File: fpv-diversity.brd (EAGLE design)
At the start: 56 x 93 mm, 63 parts, among them U1 LM1881M/NOPB, U2 LM1881M/NOPB, U3 LM1881M/NOPB, U4 MAX4545CAP+, U5 LT6206CMS8PBF, U6 LM1117IMP-5.0-NOPB

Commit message: more updates
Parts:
- R13, R2, R9: device rcl:R1206 -> rcl:R0805

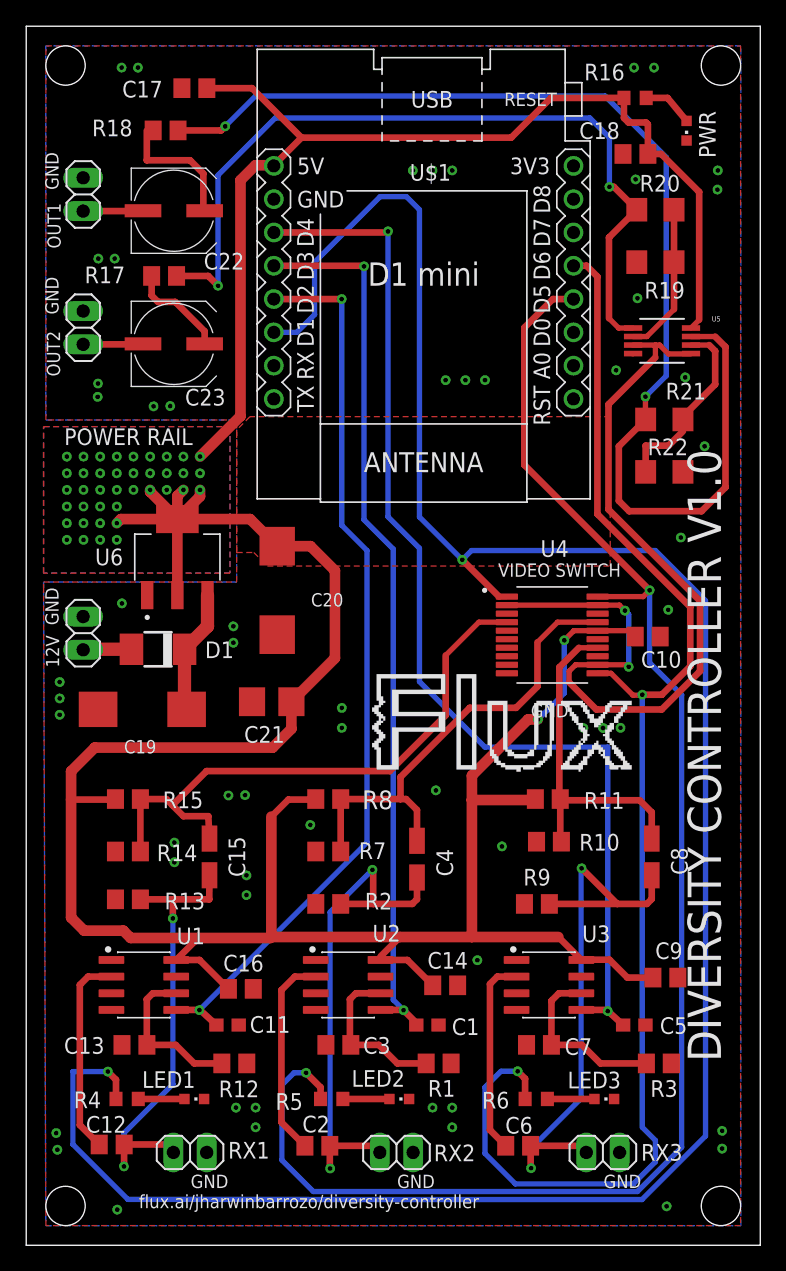
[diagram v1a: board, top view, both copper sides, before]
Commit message: board gerber updates
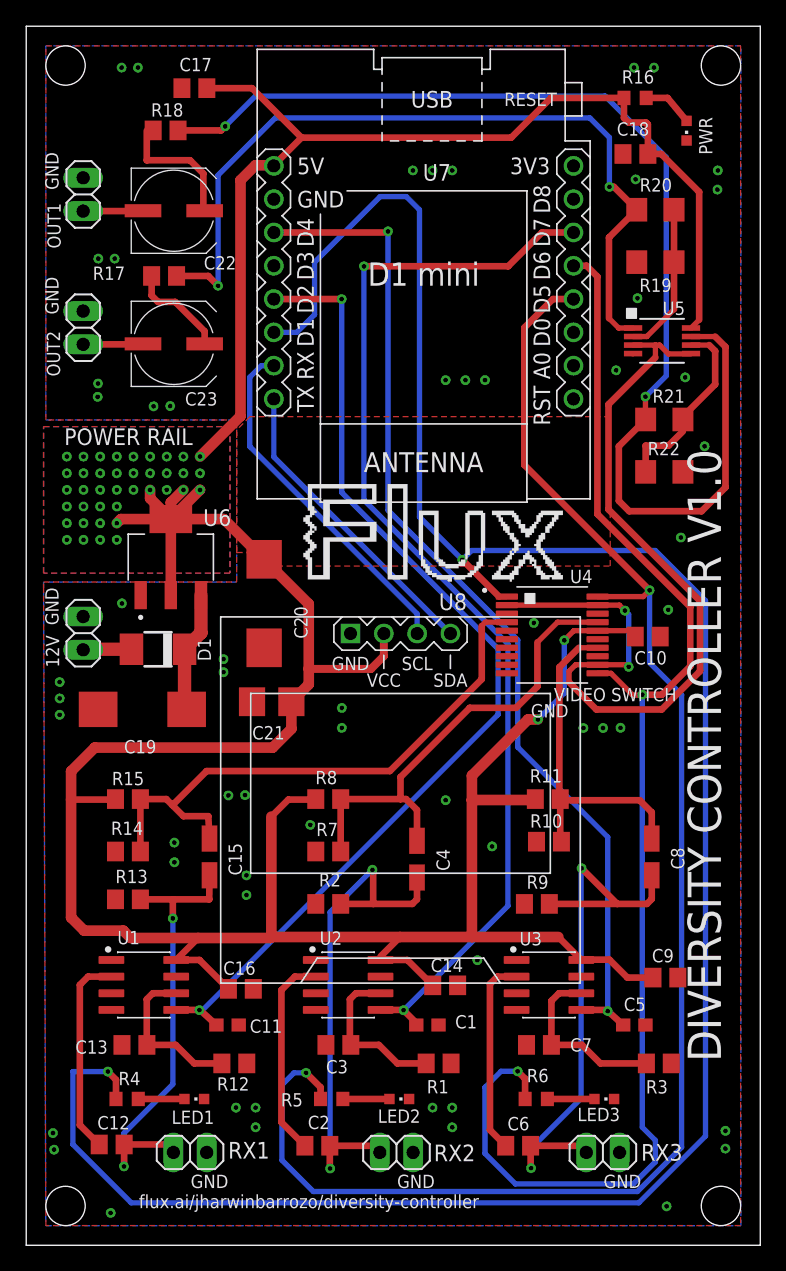
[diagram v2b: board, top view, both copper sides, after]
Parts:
- added U8: DISPLAY-OLED-128X64-I2C, DISPLAY-OLED-128X64-I2C-3D:DISPLAY-OLED-128X64-I2C
- moved C20 1.41 mm to (18.1, 49.0)
- moved U6 0.50 mm to (11.0, 52.5)
- renumbered U$1 to U7
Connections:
- new net SCL: U7.JP2.2, U8.3
- new net SDA: U7.JP2.1, U8.4
- net 5V: now also U8.2
- net BPOUT2: now also U7.JP1.6; no longer U7.JP2.5
- net GND: now also U8.1
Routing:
- net SCL: track 0.00 -> 27.0 mm
- net SDA: track 0.00 -> 23.5 mm
- net BPOUT2: track 68.3 -> 85.1 mm
- net BPOUT1: track 69.0 -> 77.5 mm
- net BPOUT3: track 84.3 -> 78.8 mm
- net 5V: track 274.3 -> 278.4 mm
- net GND: vias 58 -> 59
